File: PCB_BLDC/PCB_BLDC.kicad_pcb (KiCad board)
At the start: 2 copper layers, 22 parts, among them Q1 IRF4905, SW1 Rotary_Encoder, U1 LF15_TO220, U2 BTN8962TA, U3 BTN8962TA, U4 BTN8962TA

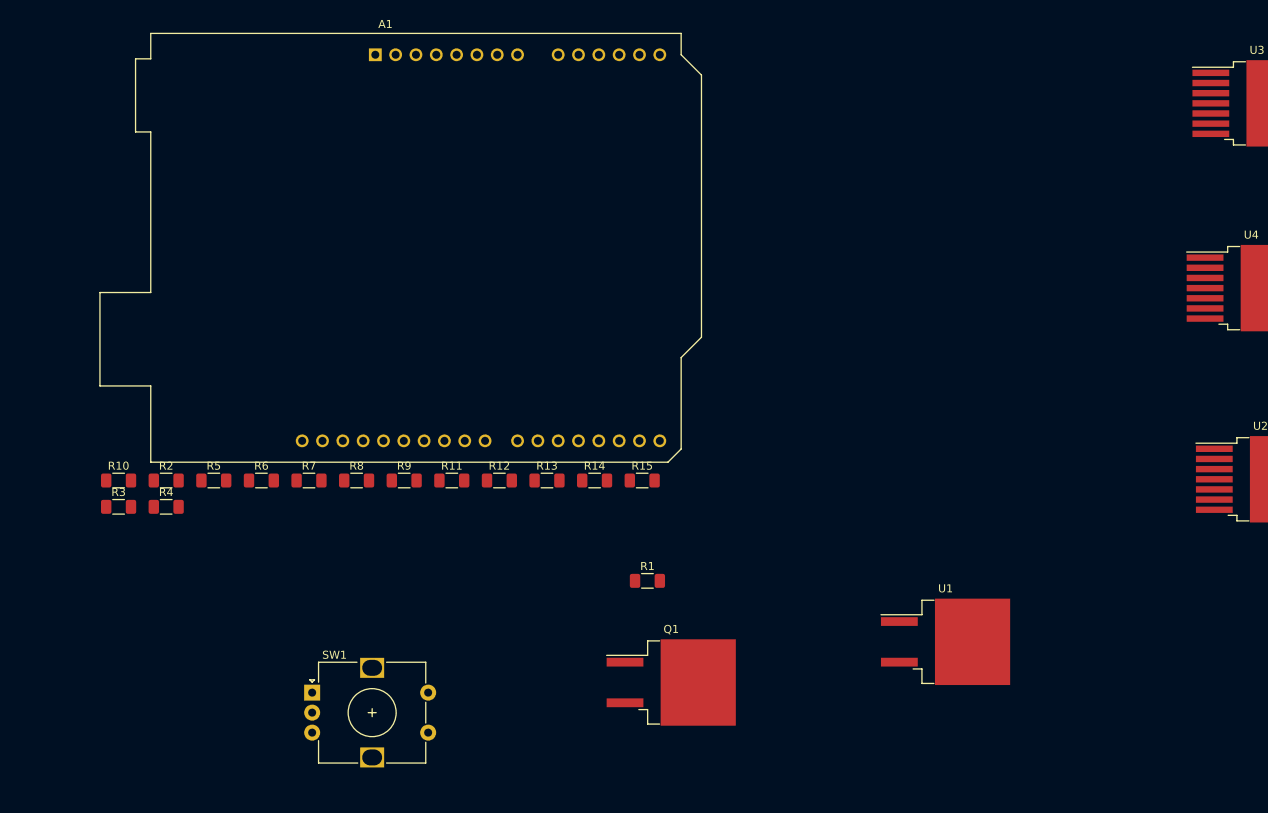
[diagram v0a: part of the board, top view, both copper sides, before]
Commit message: Main: Improve Schematic
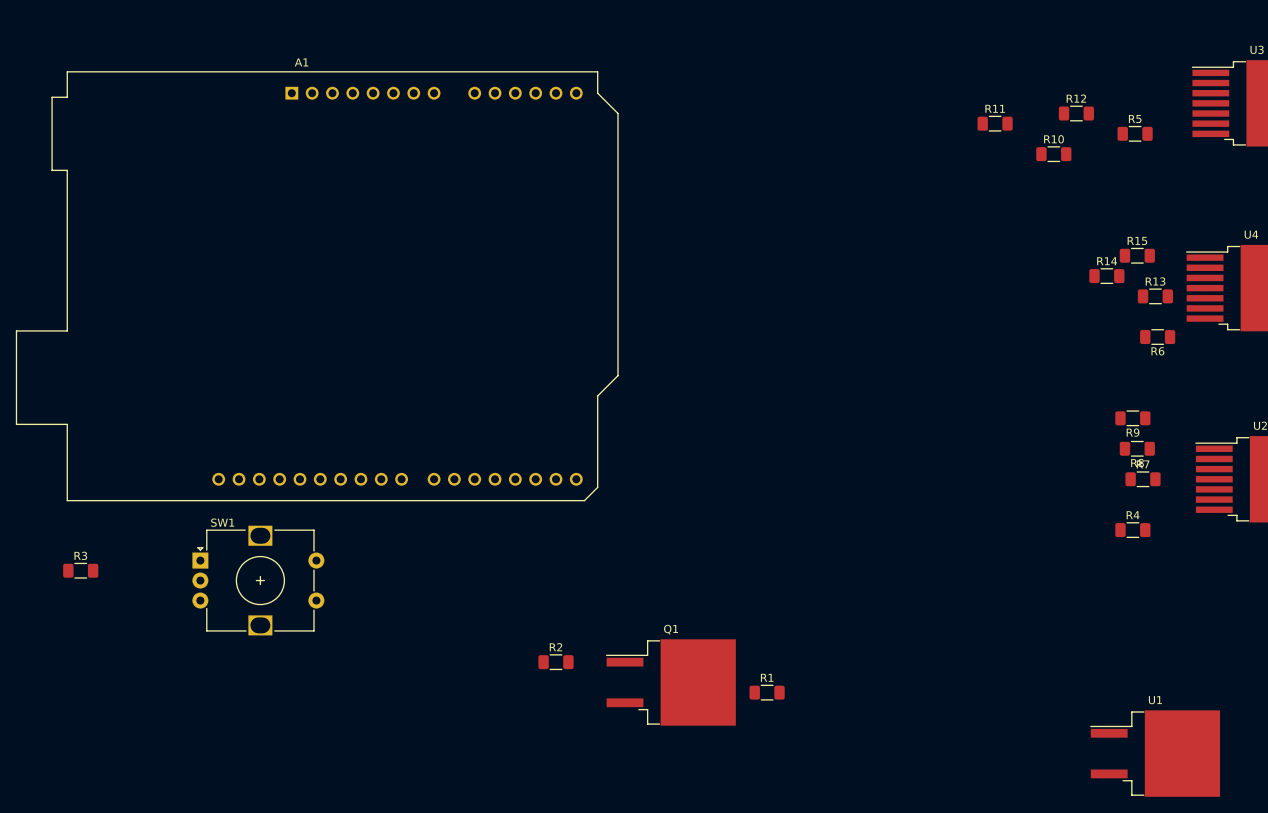
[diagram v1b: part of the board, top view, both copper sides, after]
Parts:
- moved R10 123.8 mm to (174.0, 27.9)
- moved R5 123.0 mm to (184.2, 25.4)
- moved R4 120.9 mm to (183.9, 74.9)
- moved R6 113.5 mm to (187.0, 50.8), turned to 180 degrees
- moved R7 104.3 mm to (185.1, 68.6)
- moved R8 97.7 mm to (184.4, 64.8), turned to 180 degrees
- moved R9 91.4 mm to (183.9, 61.0), turned to 180 degrees
- moved R12 85.5 mm to (176.8, 22.9)
- moved R11 81.3 mm to (166.7, 24.1)
- moved R13 79.5 mm to (186.7, 45.7)
- moved R14 68.9 mm to (180.6, 43.2)
- moved R15 68.0 mm to (184.4, 40.6)
- moved R2 53.8 mm to (111.8, 91.4)
- moved U1 29.7 mm to (186.7, 102.9)
- moved SW1 21.6 mm to (67.3, 78.7)
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
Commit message: Main: Update Schematic
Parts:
- added C1: 10uF, Capacitor_SMD:C_1206_3216Metric_Pad1.33x1.80mm_HandSolder, F.Cu at (111.8, 99.1)
- added C10: 1nF, Capacitor_SMD:C_1206_3216Metric_Pad1.33x1.80mm_HandSolder, F.Cu at (271.8, 102.1)
- added C11: 100nF, Capacitor_SMD:C_1206_3216Metric_Pad1.33x1.80mm_HandSolder, F.Cu at (248.4, 52.7)
- added C12: 100nF, Capacitor_SMD:C_1206_3216Metric_Pad1.33x1.80mm_HandSolder, F.Cu at (177.8, 33.0)
- added C13: 100nF, Capacitor_SMD:C_1206_3216Metric_Pad1.33x1.80mm_HandSolder, F.Cu at (216.2, 48.3)
- added C14: 220nF, Capacitor_SMD:C_Elec_5x5.4, F.Cu at (264.6, 103.9)
- added C15: 220nF, Capacitor_SMD:C_Elec_5x5.4, F.Cu at (241.2, 53.1)
- added C16: 220nF, Capacitor_SMD:C_Elec_5x5.4, F.Cu at (317.2, 18.6)
- added C17: 220nF, Capacitor_SMD:C_Elec_5x5.4, F.Cu at (306.8, 25.5)
- added C18: 220nF, Capacitor_SMD:C_Elec_5x5.4, F.Cu at (256.1, 103.9)
- added C19: 220nF, Capacitor_SMD:C_Elec_5x5.4, F.Cu at (241.2, 46.3)
- added C2: 10uF, Capacitor_SMD:C_1206_3216Metric_Pad1.33x1.80mm_HandSolder, F.Cu at (314.0, 30.6)
- added C20: 100nF, Capacitor_SMD:C_Elec_5x5.4, F.Cu at (242.6, 68.6)
- added C21: 100nF, Capacitor_SMD:C_Elec_5x5.4, F.Cu at (258.4, 110.7)
- added C22: 100nF, Capacitor_SMD:C_Elec_5x5.4, F.Cu at (241.2, 39.4)
- added C23: 470nF, Capacitor_SMD:C_Elec_5x5.4, F.Cu at (306.8, 32.3)
- added C24: 470nF, Capacitor_SMD:C_Elec_5x5.4, F.Cu at (315.2, 25.5)
- added C25: 470nF, Capacitor_SMD:C_Elec_5x5.4, F.Cu at (325.7, 19.8)
- added C3: 1500uF, Capacitor_SMD:CP_Elec_16x17.5, F.Cu at (-24.0, 52.1)
- added C4: 10uF, Capacitor_SMD:C_1206_3216Metric_Pad1.33x1.80mm_HandSolder, F.Cu at (265.6, 109.0)
- added C5: 1500uF, Capacitor_SMD:CP_Elec_16x17.5, F.Cu at (-22.8, 25.4)
- added C6: 1uF, Capacitor_SMD:C_1206_3216Metric_Pad1.33x1.80mm_HandSolder, F.Cu at (322.5, 24.9)
- added C7: 1uF, Capacitor_SMD:C_1206_3216Metric_Pad1.33x1.80mm_HandSolder, F.Cu at (265.6, 112.3)
- added C8: 1nF, Capacitor_SMD:C_1206_3216Metric_Pad1.33x1.80mm_HandSolder, F.Cu at (314.0, 33.9)
- added C9: 1nF, Capacitor_SMD:C_1206_3216Metric_Pad1.33x1.80mm_HandSolder, F.Cu at (311.6, 37.4)
- added D1: 12V, Diode_SMD:D_SOD-123, F.Cu at (122.8, 71.1)
- added D2: D_Schottky, Diode_SMD:D_SMB_Handsoldering, F.Cu at (57.1, 119.4)
- added D3: LED, LED_SMD:LED_1206_3216Metric_Pad1.42x1.75mm_HandSolder, F.Cu at (271.8, 105.5)
- added J1: Conn_01x01_Female, Connector_Pin:Pin_D1.0mm_L10.0mm, F.Cu at (316.6, 37.6)
- added J2: Conn_01x01_Female, Connector_Pin:Pin_D1.0mm_L10.0mm, F.Cu at (323.1, 32.8)
- added J3: Conn_01x01_Female, Connector_Pin:Pin_D1.0mm_L10.0mm, F.Cu at (319.1, 32.8)
- added J4: Conn_01x01_Female, Connector_Pin:Pin_D1.0mm_L10.0mm, F.Cu at (327.4, 28.6)
- added J5: Conn_01x01_Female, Connector_Pin:Pin_D1.0mm_L10.0mm, F.Cu at (70.4, 38.0)
- added J6: Conn_01x01_Female, Connector_Pin:Pin_D1.0mm_L10.0mm, F.Cu at (270.6, 112.5)
- added J7: Conn_01x01_Female, Connector_Pin:Pin_D1.0mm_L10.0mm, F.Cu at (320.7, 36.9)
- added J8: VCC_Unregulated, Connector:Banana_Jack_1Pin, F.Cu at (61.0, 0.00)
- added J9: VCC_GND, Connector:Banana_Jack_1Pin, F.Cu at (17.8, 1.27)
- added L1: 22uH, Inductor_SMD:L_1210_3225Metric_Pad1.42x2.65mm_HandSolder, F.Cu at (322.4, 28.7)
- added R16: 10k, Resistor_SMD:R_1206_3216Metric_Pad1.30x1.75mm_HandSolder, F.Cu at (271.8, 108.8)
- added R17: 10k, Resistor_SMD:R_1206_3216Metric_Pad1.30x1.75mm_HandSolder, F.Cu at (265.6, 115.7)
- U1: value LF15_TO220 -> MagI3C WPMDH1100XX1S / 173010542
- moved A1 41.4 mm to (118.1, 7.62)
- moved R3 30.1 mm to (34.3, 104.1)
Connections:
- Q1 pad 2: GND -> VCC
- R2 pad 1: Net-(C1-Pad1) -> /VCC_Polartiy_Check
- U1 pad 2: Net-(C4-Pad2) -> GND

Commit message: Main: Update Schmeatics and PCB
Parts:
- added J10: Conn_01x01_Female, Connector_Pin:Pin_D1.0mm_L10.0mm, F.Cu at (219.5, -107.7)
- added J11: Conn_01x01_Female, Connector_Pin:Pin_D1.0mm_L10.0mm, F.Cu at (247.9, -28.4)
- added J12: Conn_01x01_Female, Connector_Pin:Pin_D1.0mm_L10.0mm, F.Cu at (307.8, -113.3)
- added J13: Conn_01x01_Female, Connector_Pin:Pin_D1.0mm_L10.0mm, F.Cu at (253.5, -73.7)
- added J14: Conn_01x01_Female, Connector_Pin:Pin_D1.0mm_L10.0mm, F.Cu at (335.3, -79.3)
- added J15: Conn_01x01_Female, Connector_Pin:Pin_D1.0mm_L10.0mm, F.Cu at (311.9, -113.3)
- added J16: Conn_01x01_Female, Connector_Pin:Pin_D1.0mm_L10.0mm, F.Cu at (335.3, -75.2)
- added J17: Conn_01x01_Female, Connector_Pin:Pin_D1.0mm_L10.0mm, F.Cu at (339.3, -79.3)
- added J18: Conn_01x01_Female, Connector_Pin:Pin_D1.0mm_L10.0mm, F.Cu at (315.9, -113.3)
- added J19: Conn_01x01_Female, Connector_Pin:Pin_D1.0mm_L10.0mm, F.Cu at (1.02, 132.6)
- added J20: Conn_01x01_Female, Connector_Pin:Pin_D1.0mm_L10.0mm, F.Cu at (343.4, -79.3)
- added REF**: PinHeader_1x10_P2.54mm_Vertical, Connector_PinHeader_2.54mm:PinHeader_1x10_P2.54mm_Vertical, F.Cu at (109.2, 61.0)
- added REF**: PinHeader_1x08_P2.54mm_Vertical, Connector_PinHeader_2.54mm:PinHeader_1x08_P2.54mm_Vertical, F.Cu at (136.7, 60.5)
- added REF**: PinHeader_1x08_P2.54mm_Vertical, Connector_PinHeader_2.54mm:PinHeader_1x08_P2.54mm_Vertical, F.Cu at (118.9, 1.52)
- added REF**: PinHeader_1x06_P2.54mm_Vertical, Connector_PinHeader_2.54mm:PinHeader_1x06_P2.54mm_Vertical, F.Cu at (141.2, 2.54)
- L1: footprint Inductor_SMD:L_1210_3225Metric_Pad1.42x2.65mm_HandSolder -> Inductor_SMD:L_Wuerth_WE-PD-Typ-LS_Handsoldering
- Q1: footprint Package_TO_SOT_SMD:TO-263-2_TabPin1 -> Package_TO_SOT_SMD:TO-263-2
- U1: footprint Package_TO_SOT_SMD:TO-263-2_TabPin1 -> Package_SIP:SIP3_11.6x8.5mm
- U2, U3, U4: footprint Package_TO_SOT_SMD:TO-263-7_TabPin4 -> Package_TO_SOT_SMD:TO-263-7_TabPin8
- moved C6 347.7 mm to (-2.54, 148.3), turned to 270 degrees
- moved L1 322.0 mm to (1.05, 48.3), turned to 180 degrees
- moved C2 320.5 mm to (-5.08, 60.7), turned to 270 degrees
- moved R16 274.9 mm to (-2.54, 127.3), turned to 270 degrees
- moved R17 269.3 mm to (-2.54, 140.7), turned to 270 degrees
- moved C7 268.3 mm to (-2.54, 119.7), turned to 90 degrees
- moved C4 259.0 mm to (11.4, 59.4), turned to 270 degrees
- moved J5 225.7 mm to (275.8, -55.4)
- moved J4 221.1 mm to (149.2, 159.4)
- moved C14 179.8 mm to (239.3, -74.2)
- moved R8 161.8 mm to (212.9, -94.5), turned to 90 degrees
- moved R9 159.6 mm to (220.0, -94.5), turned to 90 degrees
- moved U2 159.0 mm to (240.5, -85.1)
- moved C20 153.5 mm to (224.0, -83.8), turned to 90 degrees
- moved C23 149.3 mm to (212.3, -83.3), turned to 90 degrees
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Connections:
- A1 pad 10: Net-(A1-Pad10) -> /L2_Sense
- A1 pad 11: Net-(A1-Pad11) -> /L3_Sense
- A1 pad 17: Net-(A1-Pad17) -> /L1_IN
- A1 pad 18: Net-(A1-Pad18) -> /L2_IN
- A1 pad 19: Net-(A1-Pad19) -> /L3_IN
- A1 pad 20: Net-(A1-Pad20) -> /L1_INH
- A1 pad 21: Net-(A1-Pad21) -> /L2_INH
- A1 pad 22: Net-(A1-Pad22) -> /L3_INH
- A1 pad 23: Net-(A1-Pad23) -> /L1_IS
- A1 pad 24: Net-(A1-Pad24) -> /L2_IS
- A1 pad 25: Net-(A1-Pad25) -> /L3_IS
- A1 pad 27: Net-(A1-Pad27) -> /Rot_B_Pull_Up
- A1 pad 28: Net-(A1-Pad28) -> /Rot_A_Pull_Up
- A1 pad 29: Net-(A1-Pad29) -> GND
- A1 pad 6: Net-(A1-Pad6) -> GND
- A1 pad 7: Net-(A1-Pad7) -> GND
- A1 pad 8: Net-(A1-Pad8) -> /VCC_5V
- A1 pad 9: Net-(A1-Pad9) -> /L1_Sense
- C1 pad 2: Net-(C1-Pad2) -> GND
- C15 pad 2: Net-(C15-Pad2) -> GND
- C17 pad 2: Net-(C17-Pad2) -> GND
- C19 pad 2: Net-(C19-Pad2) -> GND
- C2 pad 1: Net-(C2-Pad1) -> /VCC_Filtered
- C2 pad 2: Net-(C1-Pad2) -> GND
- C20 pad 2: Net-(C15-Pad2) -> GND
- C21 pad 2: Net-(C17-Pad2) -> GND
- C22 pad 2: Net-(C19-Pad2) -> GND
- C23 pad 2: Net-(C15-Pad2) -> GND
- C24 pad 2: Net-(C17-Pad2) -> GND
- C25 pad 2: Net-(C19-Pad2) -> GND
- C3 pad 1: Net-(C2-Pad1) -> /VCC_Filtered
- C3 pad 2: Net-(C1-Pad2) -> GND
- C4 pad 2: Net-(C1-Pad2) -> GND
- C5 pad 1: Net-(C2-Pad1) -> /VCC_Filtered
- C5 pad 2: Net-(C1-Pad2) -> GND
- J8 pad 1: Net-(J8-Pad1) -> /VCC_Unregulated
- L1 pad 2: Net-(C2-Pad1) -> /VCC_Filtered
- Q1 pad 2: VCC -> /VCC_Unregulated
- R11 pad 2: Net-(R11-Pad2) -> /L2_INH
- R14 pad 2: Net-(R14-Pad2) -> /L3_INH
- R16 pad 1: /Pull_Up_Ard_A -> /Rot_A_Pull_Up
- R17 pad 1: /Pull_Up_Ard_B -> /Rot_B_Pull_Up
- R8 pad 2: Net-(R8-Pad2) -> /L1_INH
- SW1 pad A: /Pull_Up_Ard_A -> /Rot_A_Pull_Up
- SW1 pad B: /Pull_Up_Ard_B -> /Rot_B_Pull_Up
- U2 pad 1: Net-(C15-Pad2) -> GND
- U3 pad 1: Net-(C17-Pad2) -> GND
- U4 pad 1: Net-(C19-Pad2) -> GND

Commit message: Main: Trace Routing @ PCB
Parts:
- removed J18, J19, J20: Conn_01x01_Female, Connector_Pin:Pin_D1.0mm_L10.0mm
- removed REF**: PinHeader_1x10_P2.54mm_Vertical, Connector_PinHeader_2.54mm:PinHeader_1x10_P2.54mm_Vertical
- removed REF** (x2): PinHeader_1x08_P2.54mm_Vertical, Connector_PinHeader_2.54mm:PinHeader_1x08_P2.54mm_Vertical
- removed REF**: PinHeader_1x06_P2.54mm_Vertical, Connector_PinHeader_2.54mm:PinHeader_1x06_P2.54mm_Vertical
- A1: moved to B.Cu
- J10: value Conn_01x01_Female -> Conn_01x06; footprint Connector_Pin:Pin_D1.0mm_L10.0mm -> Connector_PinHeader_2.54mm:PinHeader_1x06_P2.54mm_Vertical
- J11, J14: value Conn_01x01_Female -> Conn_01x08; footprint Connector_Pin:Pin_D1.0mm_L10.0mm -> Connector_PinHeader_2.54mm:PinHeader_1x08_P2.54mm_Vertical
- J12: value Conn_01x01_Female -> Conn_01x06; footprint Connector_Pin:Pin_D1.0mm_L10.0mm -> Connector_PinSocket_2.54mm:PinSocket_1x06_P2.54mm_Vertical
- J13, J16: value Conn_01x01_Female -> Conn_01x08; footprint Connector_Pin:Pin_D1.0mm_L10.0mm -> Connector_PinSocket_2.54mm:PinSocket_1x08_P2.54mm_Vertical
- J15: value Conn_01x01_Female -> Conn_01x10; footprint Connector_Pin:Pin_D1.0mm_L10.0mm -> Connector_PinHeader_2.54mm:PinHeader_1x10_P2.54mm_Vertical
- J17: value Conn_01x01_Female -> Conn_01x10; footprint Connector_Pin:Pin_D1.0mm_L10.0mm -> Connector_PinSocket_2.54mm:PinSocket_1x10_P2.54mm_Vertical
- moved J14 280.8 mm to (54.6, -89.6)
- moved J16 276.4 mm to (59.3, -89.6)
- moved J17 259.9 mm to (83.8, -31.8), turned to 90 degrees
- moved J15 247.2 mm to (81.3, -24.1), turned to 90 degrees
- moved J12 240.5 mm to (68.5, -89.6)
- moved J11 211.6 mm to (45.4, -89.6)
- moved J13 204.1 mm to (50.0, -89.6)
- moved J5 165.5 mm to (127.5, 18.0)
- moved J6 163.0 mm to (119.6, 17.3)
- moved J7 159.7 mm to (112.8, 16.8)
- moved J10 156.6 mm to (63.9, -89.6)
- moved R15 97.8 mm to (150.9, 66.1), turned to 270 degrees
- moved R14 86.9 mm to (156.0, 66.1), turned to 270 degrees
- moved C13 85.2 mm to (161.5, 66.1)
- moved R13 85.1 mm to (167.1, 66.1)
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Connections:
- C15 pad 1: /L1_Motor -> GND
- C15 pad 2: GND -> /L1_Motor
- C17 pad 1: /L2_Motor -> GND
- C17 pad 2: GND -> /L2_Motor
- C19 pad 1: /L3_Motor -> GND
- C19 pad 2: GND -> /L3_Motor
- J10 pad 1: /L1_IN -> Net-(J10-Pad1)
- J11 pad 1: /L2_IN -> Net-(J11-Pad1)
- J12 pad 1: /L3_IN -> Net-(J12-Pad1)
- J13 pad 1: /L1_IS -> Net-(J13-Pad1)
- J14 pad 1: /L2_IS -> Net-(J14-Pad1)
- J15 pad 1: /L3_IS -> Net-(J15-Pad1)
- J16 pad 1: /L1_INH -> Net-(J16-Pad1)
- J17 pad 1: /L2_INH -> Net-(J17-Pad1)
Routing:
- net /L3_Motor: track 0.00 -> 37.7 mm
- net Net-(R15-Pad1): track 0.00 -> 36.8 mm, vias 0 -> 2
- net GND: track 0.00 -> 34.7 mm
- net /VCC_Filtered: track 0.00 -> 32.9 mm
- net Net-(R14-Pad1): track 0.00 -> 30.9 mm, vias 0 -> 2
- net Net-(C13-Pad1): track 0.00 -> 27.4 mm, vias 0 -> 2
- net /Rot_A_Pull_Up: track 0.00 -> 17.4 mm
- net Net-(D1-Pad2): track 0.00 -> 15.6 mm
- net /VCC_5V: track 0.00 -> 15.5 mm
- net /L3_IS: track 0.00 -> 15.1 mm, vias 0 -> 2
- net /VCC_Polartiy_Check: track 0.00 -> 13.5 mm
- net Net-(D2-Pad1): track 0.00 -> 11.4 mm
- net /Rot_B_Pull_Up: track 0.00 -> 7.73 mm
- net Net-(C7-Pad1): track 0.00 -> 4.50 mm
- net Net-(C6-Pad1): track 0.00 -> 4.50 mm
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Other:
- board outline added: 152.4 x 119.4 mm
